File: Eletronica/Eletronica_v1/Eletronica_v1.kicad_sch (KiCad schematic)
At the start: 1 part

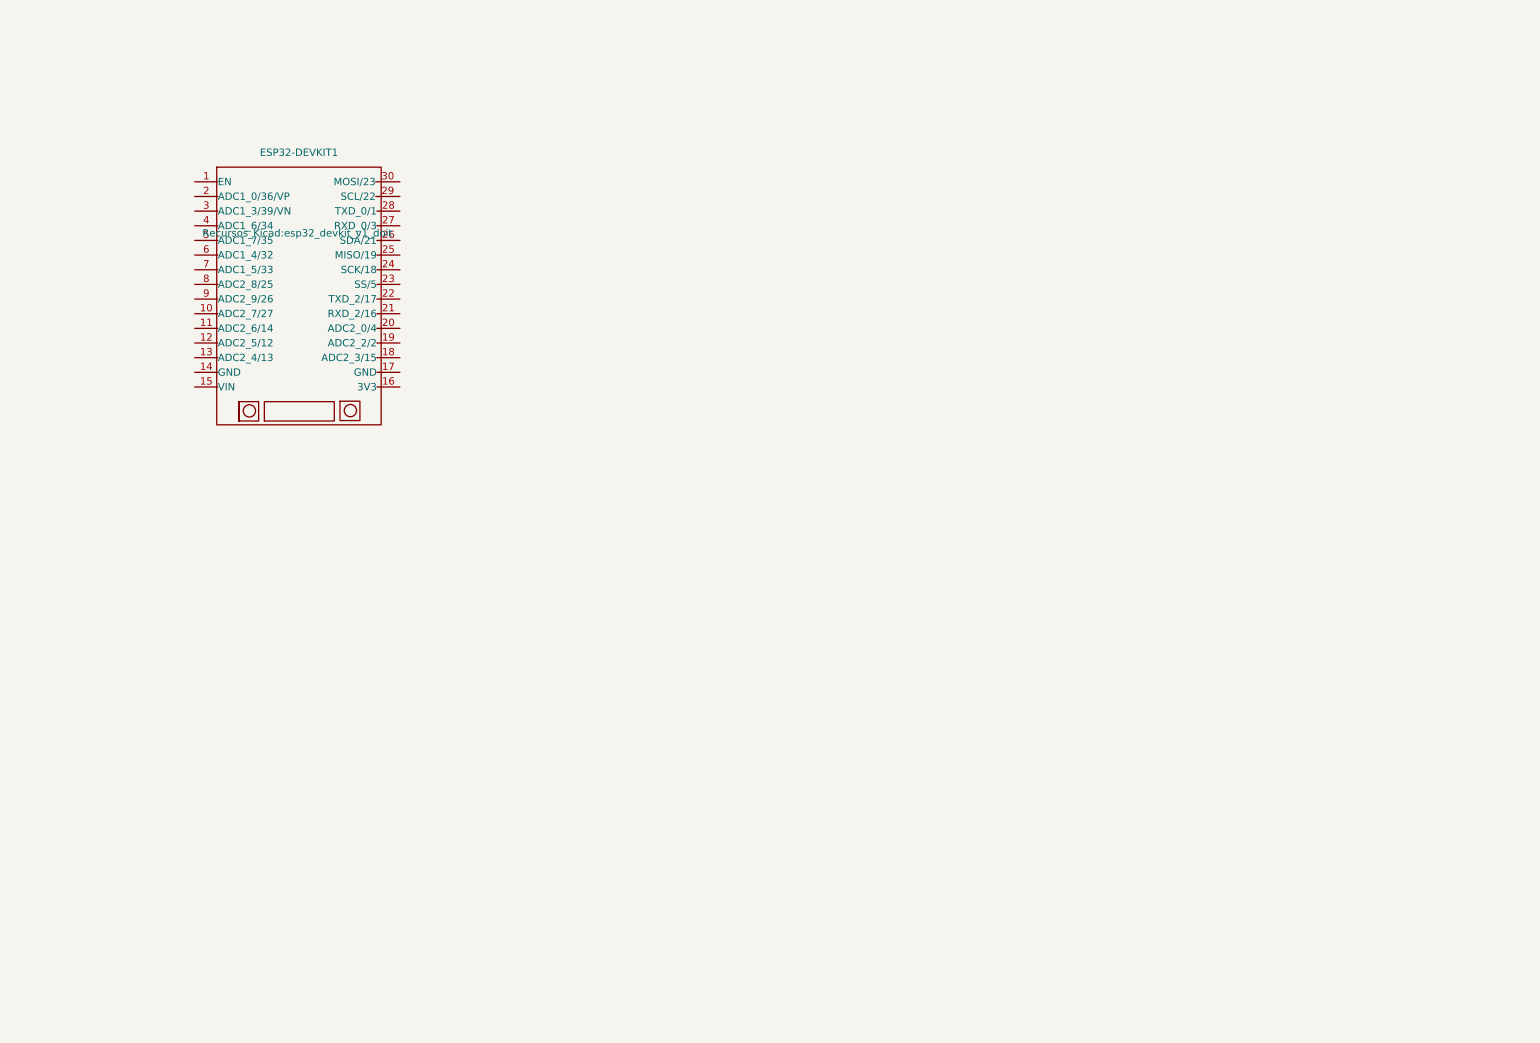
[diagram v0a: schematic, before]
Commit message: Corrigido circuito de alimentação e conexão dos periféricos
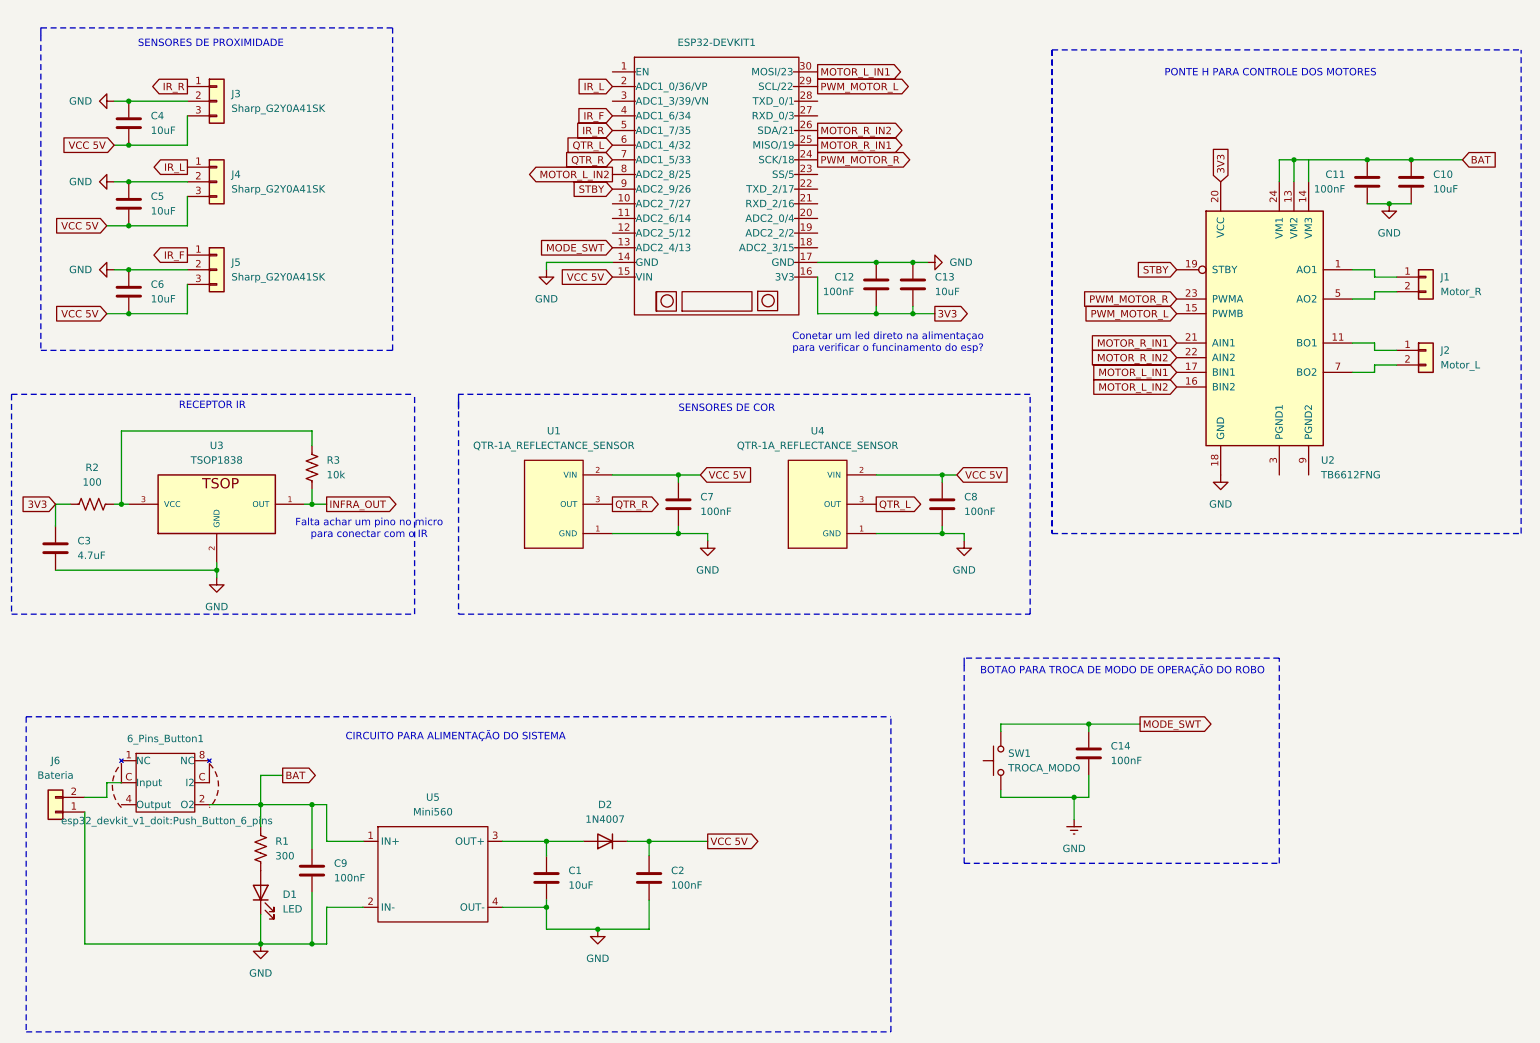
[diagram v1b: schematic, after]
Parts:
- added 6_Pins_Button1: (no value), esp32_devkit_v1_doit:Push_Button_6_pins, symbol esp32_devkit_v1_doit:Button_6_Pins
- added C1, C10, C13, C4, C5, C6: 10uF, symbol Device:C
- added C11, C12, C14, C2, C7, C8, C9: 100nF, symbol Device:C
- added C3: 4.7uF, symbol Device:C
- added D1: LED, symbol Device:LED
- added D2: 1N4007, Diode_THT:D_DO-41_SOD81_P10.16mm_Horizontal, symbol Diode:1N4007
- added J1: Motor_R, symbol Connector_Generic:Conn_01x02
- added J2: Motor_L, symbol Connector_Generic:Conn_01x02
- added J3, J4, J5: Sharp_G2Y0A41SK, symbol Connector_Generic:Conn_01x03
- added J6: Bateria, symbol Connector_Generic:Conn_01x02
- added R1: 300, symbol Device:R_US
- added R2: 100, symbol Device:R_US
- added R3: 10k, symbol Device:R_US
- added SW1: TROCA_MODO, symbol Switch:SW_Push
- added U1, U4: QTR-1A_REFLECTANCE_SENSOR, QTR-1A_REFLECTANCE_SENSOR:SENSOR_QTR-1A_REFLECTANCE_SENSOR, symbol QTR-1A_REFLECTANCE_SENSOR:QTR-1A_REFLECTANCE_SENSOR
- added U2: TB6612FNG, Package_SO:SSOP-24_5.3x8.2mm_P0.65mm, symbol Driver_Motor:TB6612FNG
- added U3: TSOP1838, TSOP1838:TSOP1838, symbol TSOP1838:TSOP1838
- added U5: Mini560, symbol Mini560:Mini560
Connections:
- net MODE_SWT: now reaches ESP32-DEVKIT1.13 (ADC2_4/13)
- net MODE_SWT: now also C14.1, SW1.2
- net GND: now reaches ESP32-DEVKIT1.14 (GND)
- net GND: now also ESP32-DEVKIT1.17 (GND), C1.2, C10.2, C11.2, C12.1, C13.1, C14.2, C2.2, C3.2, C4.1, C5.1, C6.1, C7.2, C8.2, C9.2, D1.1 (K), J3.2 (Pin_2), J4.2 (Pin_2), J5.2 (Pin_2), J6.1 (Pin_1), SW1.1, U1.1 (GND), U2.18 (GND), U3.2 (GND), U4.1 (GND), U5.2 (IN-), U5.4 (OUT-)
- net VCC 5V: now reaches ESP32-DEVKIT1.15 (VIN)
- net VCC 5V: now also C2.1, C4.2, C5.2, C6.2, C7.1, C8.1, D2.1 (K), J3.3 (Pin_3), J4.3 (Pin_3), J5.3 (Pin_3), U1.2 (VIN), U4.2 (VIN)
- net 3V3: now reaches ESP32-DEVKIT1.16 (3V3)
- net 3V3: now also C12.2, C13.2, C3.1, R2.1, U2.20 (VCC)
- net IR_L: now reaches ESP32-DEVKIT1.2 (ADC1_0/36/VP)
- net IR_L: now also J4.1 (Pin_1)
- net PWM_MOTOR_R: now reaches ESP32-DEVKIT1.24 (SCK/18)
- net PWM_MOTOR_R: now also U2.23 (PWMA)
- net MOTOR_R_IN1: now reaches ESP32-DEVKIT1.25 (MISO/19)
- net MOTOR_R_IN1: now also U2.21 (AIN1)
- net MOTOR_R_IN2: now reaches ESP32-DEVKIT1.26 (SDA/21)
- net MOTOR_R_IN2: now also U2.22 (AIN2)
- net PWM_MOTOR_L: now reaches ESP32-DEVKIT1.29 (SCL/22)
- net PWM_MOTOR_L: now also U2.15 (PWMB)
- net MOTOR_L_IN1: now reaches ESP32-DEVKIT1.30 (MOSI/23)
- net MOTOR_L_IN1: now also U2.17 (BIN1)
- net IR_F: now reaches ESP32-DEVKIT1.4 (ADC1_6/34)
- net IR_F: now also J5.1 (Pin_1)
- net IR_R: now reaches ESP32-DEVKIT1.5 (ADC1_7/35)
- net IR_R: now also J3.1 (Pin_1)
- net QTR_L: now reaches ESP32-DEVKIT1.6 (ADC1_4/32)
- net QTR_L: now also U4.3 (OUT)
- net QTR_R: now reaches ESP32-DEVKIT1.7 (ADC1_5/33)
- net QTR_R: now also U1.3 (OUT)
- net MOTOR_L_IN2: now reaches ESP32-DEVKIT1.8 (ADC2_8/25)
- net MOTOR_L_IN2: now also U2.16 (BIN2)
- net STBY: now reaches ESP32-DEVKIT1.9 (ADC2_9/26)
- net STBY: now also U2.19 (STBY)
- new net: J1.1 (Pin_1), U2.1 (AO1), U2.2 (AO1)
- new net: J1.2 (Pin_2), U2.5 (AO2), U2.6 (AO2)
- new net: R2.2, R3.1, U3.3 (VCC)
- new net: U2.10 (PGND2), U2.9 (PGND2)
- new net: J2.1 (Pin_1), U2.11 (BO1), U2.12 (BO1)
- new net: U2.3 (PGND1), U2.4 (PGND1)
- new net: J2.2 (Pin_2), U2.7 (BO2), U2.8 (BO2)
- new net: C1.1, D2.2 (A), U5.3 (OUT+)
- new net: 6_Pins_Button1.C (I2), J6.2 (Pin_2)
- new net: D1.2 (A), R1.2
- new net BAT: 6_Pins_Button1.2 (O2), C10.1, C11.1, C9.1, R1.1, U2.13 (VM2), U2.24 (VM1), U5.1 (IN+)
- new net INFRA_OUT: R3.2, U3.1 (OUT)
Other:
- note added: "BOTAO PARA TROCA DE MODO DE OPERAÇÃO DO ROBO"
- note added: "CIRCUITO PARA ALIMENTAÇÃO DO SISTEMA"
- note added: "Conetar um led direto na alimentaçao para verificar o funcinamento do esp?"
- note added: "Falta achar um pino no micro para conectar com o IR"
- note added: "PONTE H PARA CONTROLE DOS MOTORES"
- note added: "RECEPTOR IR"
- note added: "SENSORES DE COR"
- note added: "SENSORES DE PROXIMIDADE"
- title: (none) -> ROBO TRAINEE GRUPO 1
- moved on the sheet: ESP32-DEVKIT1

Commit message: Atualizado swtich e footprints
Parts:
- removed 6_Pins_Button1: (no value), esp32_devkit_v1_doit:Push_Button_6_pins, symbol esp32_devkit_v1_doit:Button_6_Pins
- removed U2: TB6612FNG, Package_SO:SSOP-24_5.3x8.2mm_P0.65mm, symbol Driver_Motor:TB6612FNG
- added SW2: SW_SPDT, Button_Switch_THT:SW_Slide_SPDT_Straight_CK_OS102011MS2Q, symbol Switch:SW_SPDT
- added U6: ROB-14450, ROB-14450:MODULE_ROB-14450, symbol ROB-14450:ROB-14450
- C1, C10, C13, C3, C4, C5, C6: footprint (none) -> Capacitor_THT:CP_Radial_D5.0mm_P2.50mm
- C11, C12, C14, C2, C7, C8, C9: footprint (none) -> Capacitor_THT:C_Disc_D5.0mm_W2.5mm_P5.00mm
- D1: footprint (none) -> LED_THT:LED_D5.0mm
- ESP32-DEVKIT1: footprint Recursos_Kicad:esp32_devkit_v1_doit -> esp32_devkit_v1_doit:esp32_devkit_v1_doit
- J1, J2: footprint (none) -> Connector_Phoenix_MC:PhoenixContact_MC_1,5_2-G-3.5_1x02_P3.50mm_Horizontal
- J3, J4, J5: footprint (none) -> Connector_JST:JST_PH_B3B-PH-K_1x03_P2.00mm_Vertical
- J6: footprint (none) -> Connector_JST:JST_EH_B2B-EH-A_1x02_P2.50mm_Vertical
- R1, R2, R3: footprint (none) -> Resistor_THT:R_Axial_DIN0207_L6.3mm_D2.5mm_P10.16mm_Horizontal
- SW1: footprint (none) -> Button_Switch_THT:SW_Tactile_Straight_KSA0Axx1LFTR
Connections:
- net 3V3: now also U6.2 (VCC)
- net BAT: now also SW2.3 (C), U6.1 (VM)
- net GND: now also U6.3 (GND), U6.8 (GND), U6.9 (GND)
- net MOTOR_L_IN1: now also U6.12 (BI1)
- net MOTOR_L_IN2: now also U6.11 (BI2)
- net MOTOR_R_IN1: now also U6.14 (AI1)
- net MOTOR_R_IN2: now also U6.15 (AI2)
- net PWM_MOTOR_L: now also U6.10 (PWMB)
- net PWM_MOTOR_R: now also U6.16 (PWMA)
- net STBY: now also U6.13 (STBY)
- net at J1.1 (Pin_1): now also U6.4 (A01)
- net at J1.2 (Pin_2): now also U6.5 (A02)
- net at J2.1 (Pin_1): now also U6.7 (B01)
- net at J2.2 (Pin_2): now also U6.6 (B02)
- net at J6.2 (Pin_2): now also SW2.2 (B)
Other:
- note removed: "Conetar um led direto na alimentaçao para verificar o funcinamento do esp?"
- moved on the sheet: C10, C11, J1, J2

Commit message: Reduzido Capacitores, e tracado layout parcial da pcb
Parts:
- removed C10, C4, C5, C6: 10uF, Capacitor_THT:CP_Radial_D5.0mm_P2.50mm, symbol Device:C
- removed C11: 100nF, Capacitor_THT:C_Disc_D5.0mm_W2.5mm_P5.00mm, symbol Device:C
- added C4, C5, C6: 10 uF, PCM_Capacitor_THT_AKL:CP_Radial_D5.0mm_P2.50mm, symbol PCM_Capacitor_AKL:CP_Radial_D5.0mm_P2.50mm
- J1, J2: footprint Connector_Phoenix_MC:PhoenixContact_MC_1,5_2-G-3.5_1x02_P3.50mm_Horizontal -> Connector_Molex:Molex_KK-254_AE-6410-02A_1x02_P2.54mm_Vertical
- SW2: footprint Button_Switch_THT:SW_Slide_SPDT_Straight_CK_OS102011MS2Q -> Button_Switch_THT:SW_Slide-03_Wuerth-WS-SLTV_10x2.5x6.4_P2.54mm
- U5: footprint (none) -> Buck_Converter_4r7:Sem título
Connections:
- net GND: now also C4.1, C5.1, C6.1
- net VCC 5V: now also C4.2, C5.2, C6.2

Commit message: Finalizado a versao funcional da placa
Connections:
- net INFRA_OUT: now also ESP32-DEVKIT1.13 (ADC2_4/13)
- net MODE_SWT: now also ESP32-DEVKIT1.11 (ADC2_6/14); no longer ESP32-DEVKIT1.13 (ADC2_4/13)
- net MOTOR_L_IN1: now also ESP32-DEVKIT1.26 (SDA/21); no longer ESP32-DEVKIT1.30 (MOSI/23)
- net MOTOR_L_IN2: now also ESP32-DEVKIT1.27 (RXD_0/3); no longer ESP32-DEVKIT1.8 (ADC2_8/25)
- net MOTOR_R_IN1: now also ESP32-DEVKIT1.24 (SCK/18); no longer ESP32-DEVKIT1.25 (MISO/19)
- net MOTOR_R_IN2: now also ESP32-DEVKIT1.23 (SS/5); no longer ESP32-DEVKIT1.26 (SDA/21)
- net PWM_MOTOR_L: now also ESP32-DEVKIT1.28 (TXD_0/1); no longer ESP32-DEVKIT1.29 (SCL/22)
- net PWM_MOTOR_R: now also ESP32-DEVKIT1.22 (TXD_2/17); no longer ESP32-DEVKIT1.24 (SCK/18)
- net STBY: now also ESP32-DEVKIT1.25 (MISO/19); no longer ESP32-DEVKIT1.9 (ADC2_9/26)
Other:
- note removed: "Falta achar um pino no micro para conectar com o IR"
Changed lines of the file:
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@@
-		)
-	)
-	(text "Falta achar um pino no micro \npara conectar com o IR"
-		(exclude_from_sim no)
-		(at 77.216 104.648 0)
-		(effects
-			(font
-				(size 1.27 1.27)
-				(color 194 0 0 1)
-			)
 		)
 	)
@@
 	(global_label "PWM_MOTOR_R"
 		(shape output)
-		(at 154.94 40.64 0)
+		(at 154.94 45.72 0)
 		(fields_autoplaced yes)
 		(effects
@@
 		)
 		(property "Intersheetrefs" "${INTERSHEET_REFS}"
-			(at 171.6532 40.64 0)
+			(at 171.6532 45.72 0)
 			(hide yes)
 			(show_name no)
@@
 		)
 	)
-	(global_label "MOTOR_L_IN2"
+	(global_label "MOTOR_R_IN1"
 		(shape output)
-		(at 119.38 43.18 180)
-		(fields_autoplaced yes)
-		(effects
-			(font
-				(size 1.27 1.27)
-			)
-			(justify right)
-		)
-		(property "Intersheetrefs" "${INTERSHEET_REFS}"
-			(at 103.9367 43.18 0)
-			(hide yes)
-			(show_name no)
-			(do_not_autoplace no)
-			(effects
-				(font
-					(size 1.27 1.27)
-				)
-				(justify right)
+		(at 154.94 40.64 0)
+		(fields_autoplaced yes)
+		(effects
+			(font
+				(size 1.27 1.27)
+			)
+			(justify left)
+		)
+		(property "Intersheetrefs" "${INTERSHEET_REFS}"
+			(at 170.6252 40.64 0)
+			(hide yes)
+			(show_name no)
+			(do_not_autoplace no)
+			(effects
+				(font
+					(size 1.27 1.27)
+				)
+				(justify left)
 			)
 		)
@@
 	(global_label "PWM_MOTOR_L"
 		(shape output)
-		(at 154.94 27.94 0)
+		(at 154.94 30.48 0)
 		(fields_autoplaced yes)
 		(effects
@@
 		)
 		(property "Intersheetrefs" "${INTERSHEET_REFS}"
-			(at 171.4113 27.94 0)
+			(at 171.4113 30.48 0)
 			(hide yes)
 			(show_name no)
@@
 		)
 	)
-	(global_label "MOTOR_R_IN1"
-		(shape output)
-		(at 154.94 38.1 0)
-		(fields_autoplaced yes)
-		(effects
-			(font
-				(size 1.27 1.27)
-			)
-			(justify left)
-		)
-		(property "Intersheetrefs" "${INTERSHEET_REFS}"
-			(at 170.6252 38.1 0)
-			(hide yes)
-			(show_name no)
-			(do_not_autoplace no)
-			(effects
-				(font
-					(size 1.27 1.27)
-				)
-				(justify left)
-			)
-		)
-	)
-	(global_label "MOTOR_L_IN1"
-		(shape output)
-		(at 154.94 25.4 0)
-		(fields_autoplaced yes)
-		(effects
-			(font
-				(size 1.27 1.27)
-			)
-			(justify left)
-		)
-		(property "Intersheetrefs" "${INTERSHEET_REFS}"
-			(at 170.3833 25.4 0)
-			(hide yes)
-			(show_name no)
-			(do_not_autoplace no)
-			(effects
-				(font
-					(size 1.27 1.27)
-				)
-				(justify left)
-			)
-		)
-	)
 	(global_label "VCC 5V"
 		(shape input)
@@
 		)
 	)
-	(global_label "MOTOR_R_IN2"
-		(shape output)
-		(at 154.94 35.56 0)
-		(fields_autoplaced yes)
-		(effects
-			(font
-				(size 1.27 1.27)
-			)
-			(justify left)
-		)
-		(property "Intersheetrefs" "${INTERSHEET_REFS}"
-			(at 170.6252 35.56 0)
-			(hide yes)
-			(show_name no)
-			(do_not_autoplace no)
-			(effects
-				(font
-					(size 1.27 1.27)
-				)
-				(justify left)
-			)
-		)
-	)
-	(global_label "MODE_SWT"
-		(shape input)
-		(at 119.38 55.88 180)
-		(fields_autoplaced yes)
-		(effects
-			(font
-				(size 1.27 1.27)
-			)
-			(justify right)
-		)
-		(property "Intersheetrefs" "${INTERSHEET_REFS}"
-			(at 106.5978 55.88 0)
-			(hide yes)
-			(show_name no)
-			(do_not_autoplace no)
-			(effects
-				(font
-					(size 1.27 1.27)
-				)
-				(justify right)
-			)
-		)
-	)
 	(global_label "STBY"
 		(shape input)
-		(at 119.38 45.72 180)
-		(fields_autoplaced yes)
-		(effects
-			(font
-				(size 1.27 1.27)
-			)
-			(justify right)
-		)
-		(property "Intersheetrefs" "${INTERSHEET_REFS}"
-			(at 111.8591 45.72 0)
-			(hide yes)
-			(show_name no)
-			(do_not_autoplace no)
-			(effects
-				(font
-					(size 1.27 1.27)
-				)
-				(justify right)
+		(at 154.94 38.1 0)
+		(fields_autoplaced yes)
+		(effects
+			(font
+				(size 1.27 1.27)
+			)
+			(justify left)
+		)
+		(property "Intersheetrefs" "${INTERSHEET_REFS}"
+			(at 162.4609 38.1 0)
+			(hide yes)
+			(show_name no)
+			(do_not_autoplace no)
+			(effects
+				(font
+					(size 1.27 1.27)
+				)
+				(justify left)
+			)
+		)
+	)
+	(global_label "MOTOR_L_IN2"
+		(shape output)
+		(at 154.94 33.02 0)
+		(fields_autoplaced yes)
+		(effects
+			(font
+				(size 1.27 1.27)
+			)
+			(justify left)
+		)
+		(property "Intersheetrefs" "${INTERSHEET_REFS}"
+			(at 170.3833 33.02 0)
+			(hide yes)
+			(show_name no)
+			(do_not_autoplace no)
+			(effects
+				(font
+					(size 1.27 1.27)
+				)
+				(justify left)
 			)
 		)
@@
 	)
 	(global_label "MODE_SWT"
+		(shape input)
+		(at 119.38 50.8 180)
+		(fields_autoplaced yes)
+		(effects
+			(font
+				(size 1.27 1.27)
+			)
+			(justify right)
+		)
+		(property "Intersheetrefs" "${INTERSHEET_REFS}"
+			(at 106.5978 50.8 0)
+			(hide yes)
+			(show_name no)
+			(do_not_autoplace no)
+			(effects
+				(font
+					(size 1.27 1.27)
+				)
+				(justify right)
+			)
+		)
+	)
+	(global_label "MODE_SWT"
 		(shape output)
 		(at 210.82 138.43 0)
@@
 		)
 	)
+	(global_label "INFRA_OUT"
+		(shape input)
+		(at 119.38 55.88 180)
+		(fields_autoplaced yes)
+		(effects
+			(font
+				(size 1.27 1.27)
+			)
+			(justify right)
+		)
+		(property "Intersheetrefs" "${INTERSHEET_REFS}"
+			(at 106.4161 55.88 0)
+			(hide yes)
+			(show_name no)
+			(do_not_autoplace no)
+			(effects
+				(font
+					(size 1.27 1.27)
+				)
+				(justify right)
+			)
+		)
+	)
+	(global_label "MOTOR_L_IN1"
+		(shape output)
+		(at 154.94 35.56 0)
+		(fields_autoplaced yes)
+		(effects
+			(font
+				(size 1.27 1.27)
+			)
+			(justify left)
+		)
+		(property "Intersheetrefs" "${INTERSHEET_REFS}"
+			(at 170.3833 35.56 0)
+			(hide yes)
+			(show_name no)
+			(do_not_autoplace no)
+			(effects
+				(font
+					(size 1.27 1.27)
+				)
+				(justify left)
+			)
+		)
+	)
 	(global_label "IR_F"
 		(shape input)
@@
 			)
 		)
+	)
+	(global_label "MOTOR_R_IN2"
+		(shape output)
+		(at 154.94 43.18 0)
+		(fields_autoplaced yes)
+		(effects
+			(font
+				(size 1.27 1.27)
+			)
+			(justify left)
+		)
+		(property "Intersheetrefs" "${INTERSHEET_REFS}"
+			(at 170.6252 43.18 0)
+			(hide yes)
+			(show_name no)
+			(do_not_autoplace no)
+			(effects
+				(font
+					(size 1.27 1.27)
+				)
+				(justify left)
+			)
+		)
